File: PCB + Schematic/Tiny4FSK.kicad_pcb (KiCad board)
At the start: 4 copper layers, 30.9 x 65.8 mm, 81 parts, among them IC1 SI4063, J1 SWD, J2 GPIO, J3 USBC, J4 OPTIONAL, J5 I2C, J6 Power, J7 SPI, SW1 RST, SW2 BATT PWR, U1 BME280, U2 MAX-M10S, U3 Linear Step-Down, U4 ATSAMD21G18A-A, U5 TCXO MCU, U6 TPS61200DRC

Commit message: Rebase Rev. 4 PCB files
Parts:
- removed the C11 at (151.0, 99.8)
- removed the C15 at (148.2, 112.0)
- removed the C26 at (144.1, 123.0)
- removed the C4 at (151.1, 88.4)
- removed the C5 at (151.1, 90.5)
- removed the C6 at (148.2, 93.2)
- removed the G*** at (151.2, 102.8)
- removed the G*** at (151.1, 90.5)
- removed the G*** at (142.5, 127.5)
- removed the G*** at (153.0, 127.5)
- removed the J1 at (140.0, 73.5)
- removed JP2: Source, Jumper:SolderJumper-3_P1.3mm_Open_Pad1.0x1.5mm_NumberLabels
- removed the R3 at (151.1, 92.6)
- removed the R7 at (147.7, 100.7)
- removed the U3 at (143.9, 88.1)
- added C13: 100nF, Capacitor_SMD:C_0402_1005Metric_Pad0.74x0.62mm_HandSolder, F.Cu at (158.0, 58.6)
- added C17: 100 nF, Capacitor_SMD:C_0402_1005Metric_Pad0.74x0.62mm_HandSolder, F.Cu at (127.9, 92.7)
- added C18: 1uF, Capacitor_SMD:C_0402_1005Metric_Pad0.74x0.62mm_HandSolder, F.Cu at (129.9, 92.7)
- added C19: 4.7 nF, Capacitor_SMD:C_0402_1005Metric_Pad0.74x0.62mm_HandSolder, F.Cu at (135.9, 98.0)
- added C22: 1uF, Capacitor_SMD:C_0402_1005Metric_Pad0.74x0.62mm_HandSolder, F.Cu at (132.4, 95.1)
- added C25: 100 nF, Capacitor_SMD:C_0402_1005Metric_Pad0.74x0.62mm_HandSolder, F.Cu at (130.5, 98.2)
- added C28: 1.5pF, Capacitor_SMD:C_0402_1005Metric_Pad0.74x0.62mm_HandSolder, F.Cu at (151.7, 42.9)
- added C29: 100nF, Capacitor_SMD:C_0402_1005Metric_Pad0.74x0.62mm_HandSolder, F.Cu at (150.7, 73.3)
- added C30: 100 nF, Capacitor_SMD:C_0402_1005Metric_Pad0.74x0.62mm_HandSolder, F.Cu at (143.9, 78.2)
- added G***: LOGO, LOGO, B.Cu at (144.4, 41.0)
- added G***: LOGO, LOGO, B.Cu at (149.1, 80.1)
- added G***: LOGO, LOGO, B.Cu at (159.3, 41.5)
- added G***: LOGO, LOGO, B.Cu at (149.1, 67.5)
- added G***: LOGO, LOGO, B.Cu at (144.7, 43.1)
- added G***: LOGO, LOGO, B.Cu at (144.7, 45.4)
- added J6: SPI, Connector_PinHeader_2.54mm:PinHeader_1x05_P2.54mm_Vertical, F.Cu at (160.4, 94.1)
- added J8: SWD, Connector_PinHeader_1.27mm:PinHeader_2x05_P1.27mm_Vertical_SMD, B.Cu at (144.8, 103.8)
- added L8: 3.9 nH, Inductor_SMD:L_0402_1005Metric_Pad0.77x0.64mm_HandSolder, F.Cu at (153.2, 43.7)
- added R10: 5k1, Resistor_SMD:R_0402_1005Metric_Pad0.72x0.64mm_HandSolder, F.Cu at (134.0, 98.0)
- added R11: 1M, Resistor_SMD:R_0402_1005Metric_Pad0.72x0.64mm_HandSolder, F.Cu at (136.9, 98.0)
- added R12: 5k1, Resistor_SMD:R_0402_1005Metric_Pad0.72x0.64mm_HandSolder, F.Cu at (132.9, 98.1)
- added R6: 1M, Resistor_SMD:R_0402_1005Metric_Pad0.72x0.64mm_HandSolder, F.Cu at (145.7, 75.7)
- added U7: Linear Step-Down, LDO:MCP1700, F.Cu at (133.5, 92.1)
- AE1: value GPS ANT -> 1575AT43A0040
- AE2: value ANT -> TX Antenna
- BT1: value AAA -> BK-53; footprint BatteryExtended:BAT_BK-82 -> BatteryExtended:BAT_53
- C1: value 1uF -> 10uF; footprint Capacitor_SMD:C_0805_2012Metric_Pad1.18x1.45mm_HandSolder -> Capacitor_SMD:C_0402_1005Metric_Pad0.74x0.62mm_HandSolder
- C10: renamed from C9; value 100nF -> 100 nF; footprint Capacitor_SMD:C_0805_2012Metric_Pad1.18x1.45mm_HandSolder -> Capacitor_SMD:C_0402_1005Metric_Pad0.74x0.62mm_HandSolder
- C11: renamed from C10; footprint Capacitor_SMD:C_0805_2012Metric_Pad1.18x1.45mm_HandSolder -> Capacitor_SMD:C_0402_1005Metric_Pad0.74x0.62mm_HandSolder
- C12: renamed from C7; value 100nF -> 10 uF; footprint Capacitor_SMD:C_0805_2012Metric_Pad1.18x1.45mm_HandSolder -> Capacitor_SMD:C_0402_1005Metric_Pad0.74x0.62mm_HandSolder
- C14, C2, C3: footprint Capacitor_SMD:C_0805_2012Metric_Pad1.18x1.45mm_HandSolder -> Capacitor_SMD:C_0402_1005Metric_Pad0.74x0.62mm_HandSolder
- C16: renamed from C20; footprint Capacitor_SMD:C_0603_1608Metric_Pad1.08x0.95mm_HandSolder -> Capacitor_SMD:C_0402_1005Metric_Pad0.74x0.62mm_HandSolder
- C20: renamed from C22; value 15 pF -> 8 pF; footprint Capacitor_SMD:C_0201_0603Metric_Pad0.64x0.40mm_HandSolder -> Capacitor_SMD:C_0402_1005Metric_Pad0.74x0.62mm_HandSolder
- C21: renamed from C23; footprint Capacitor_SMD:C_0805_2012Metric_Pad1.18x1.45mm_HandSolder -> Capacitor_SMD:C_0402_1005Metric_Pad0.74x0.62mm_HandSolder
- C23: renamed from C18; footprint Capacitor_SMD:C_0805_2012Metric_Pad1.18x1.45mm_HandSolder -> Capacitor_SMD:C_0402_1005Metric_Pad0.74x0.62mm_HandSolder
- C24: renamed from C25; value 12 pF -> 6 pF
- C26: renamed from C24; value 10 nF -> 100 nF; footprint Capacitor_SMD:C_0805_2012Metric_Pad1.18x1.45mm_HandSolder -> Capacitor_SMD:C_0402_1005Metric_Pad0.74x0.62mm_HandSolder
- C27: value 10 pF -> 5 pF; footprint Capacitor_SMD:C_0201_0603Metric_Pad0.64x0.40mm_HandSolder -> Capacitor_SMD:C_0402_1005Metric_Pad0.74x0.62mm_HandSolder
- C4: renamed from C17; footprint Capacitor_SMD:C_0805_2012Metric_Pad1.18x1.45mm_HandSolder -> Capacitor_SMD:C_0603_1608Metric_Pad1.08x0.95mm_HandSolder
- C5: renamed from C21; footprint Capacitor_SMD:C_0805_2012Metric_Pad1.18x1.45mm_HandSolder -> Capacitor_SMD:C_0402_1005Metric_Pad0.74x0.62mm_HandSolder
- C6: renamed from C12; value 10uF -> 100 nF; footprint Capacitor_SMD:C_0805_2012Metric_Pad1.18x1.45mm_HandSolder -> Capacitor_SMD:C_0402_1005Metric_Pad0.74x0.62mm_HandSolder
- C7: renamed from C13; value 100nF -> 10 uF; footprint Capacitor_SMD:C_0805_2012Metric_Pad1.18x1.45mm_HandSolder -> Capacitor_SMD:C_0603_1608Metric_Pad1.08x0.95mm_HandSolder
- C8: renamed from C16; footprint Capacitor_SMD:C_0805_2012Metric_Pad1.18x1.45mm_HandSolder -> Capacitor_SMD:C_0402_1005Metric_Pad0.74x0.62mm_HandSolder
- C9: renamed from C8; footprint Capacitor_SMD:C_0805_2012Metric_Pad1.18x1.45mm_HandSolder -> Capacitor_SMD:C_0402_1005Metric_Pad0.74x0.62mm_HandSolder
- J1: renamed from J6; value Power -> Power Ext
- J3: value USBC -> I2C; footprint Connector_USB:USB_C_Receptacle_GCT_USB4105-xx-A_16P_TopMnt_Horizontal -> Connector_PinHeader_2.54mm:PinHeader_1x04_P2.54mm_Vertical
- J4: value OPTIONAL -> USB; footprint Jumper:SolderJumper-2_P1.3mm_Open_Pad1.0x1.5mm -> Connector_PinHeader_2.54mm:PinHeader_1x04_P2.54mm_Vertical
- J5: value I2C -> USB Breakout
- J7: value SPI -> USBC; footprint Connector_PinHeader_2.54mm:PinHeader_1x05_P2.54mm_Vertical -> Connector_USB:USB_C_Receptacle_GCT_USB4105-xx-A_16P_TopMnt_Horizontal
- JP1: value SWITCH_EN -> Switch EN
- L1: value 33 nH -> 3.9 nH
- L3: footprint Inductor_SMD:L_0603_1608Metric_Pad1.05x0.95mm_HandSolder -> Inductor_SMD:L_0402_1005Metric_Pad0.77x0.64mm_HandSolder
- L4: value 33 nH -> 14 nH
- L5: value 30 nH -> 14 nH
- L6: value 36 nH -> 14 nH
- L7: value 22 nH -> 14 nH
- R1: renamed from R2; footprint Resistor_SMD:R_0805_2012Metric_Pad1.20x1.40mm_HandSolder -> Resistor_SMD:R_0402_1005Metric_Pad0.72x0.64mm_HandSolder
- R13: renamed from R10; value 100 -> 330; footprint Resistor_SMD:R_0805_2012Metric_Pad1.20x1.40mm_HandSolder -> Resistor_SMD:R_0402_1005Metric_Pad0.72x0.64mm_HandSolder
- R14: renamed from R13; value 1k -> 330; footprint Resistor_SMD:R_0805_2012Metric_Pad1.20x1.40mm_HandSolder -> Resistor_SMD:R_0402_1005Metric_Pad0.72x0.64mm_HandSolder
- R15: renamed from R9; value 100 -> 330; footprint Resistor_SMD:R_0805_2012Metric_Pad1.20x1.40mm_HandSolder -> Resistor_SMD:R_0402_1005Metric_Pad0.72x0.64mm_HandSolder
- R2: renamed from R1; footprint Resistor_SMD:R_0805_2012Metric_Pad1.20x1.40mm_HandSolder -> Resistor_SMD:R_0402_1005Metric_Pad0.72x0.64mm_HandSolder
- R3: renamed from R12; value 5M -> 1M; footprint Resistor_SMD:R_0805_2012Metric_Pad1.20x1.40mm_HandSolder -> Resistor_SMD:R_0402_1005Metric_Pad0.72x0.64mm_HandSolder
- R4: renamed from R11; value 900k -> 180k; footprint Resistor_SMD:R_0805_2012Metric_Pad1.20x1.40mm_HandSolder -> Resistor_SMD:R_0402_1005Metric_Pad0.72x0.64mm_HandSolder
- R5: value 5k1 -> 1M; footprint Resistor_SMD:R_0805_2012Metric_Pad1.20x1.40mm_HandSolder -> Resistor_SMD:R_0402_1005Metric_Pad0.72x0.64mm_HandSolder
- R7: renamed from R4; footprint Resistor_SMD:R_0805_2012Metric_Pad1.20x1.40mm_HandSolder -> Resistor_SMD:R_0402_1005Metric_Pad0.72x0.64mm_HandSolder
- R8: renamed from R6; footprint Resistor_SMD:R_0805_2012Metric_Pad1.20x1.40mm_HandSolder -> Resistor_SMD:R_0402_1005Metric_Pad0.72x0.64mm_HandSolder
- R9: renamed from R8; footprint Resistor_SMD:R_0805_2012Metric_Pad1.20x1.40mm_HandSolder -> Resistor_SMD:R_0402_1005Metric_Pad0.72x0.64mm_HandSolder
- SW1: renamed from SW2; value BATT PWR -> Power Switch; footprint SlideSwitch:WS-SLSU_6p7x2p7_WRE -> Button_Switch_SMD:SW_SPDT_PCM12
- U2: value MAX-M10S -> ATGM336H; footprint RF_GPS:ublox_MAX -> RF_GPS_Extended:ATGM336H
- U4: renamed from U5; value TCXO MCU -> ECS-327TXO-2012; footprint Oscillator_TCXO:ATXK-H11-E-32.768KHZ-E50-T3 -> Oscillator_TCXO:ECS-327TXO-2012
- U8: renamed from XTAL1; footprint OSC:OSC_ECS-TXO-32CSMV-260-AN-TR -> Oscillator_TCXO:ECS-TXO-20CSMV4
- moved H3 62.8 mm to (115.0, 64.7)
- moved JP1 60.3 mm to (145.4, 63.6), turned to 90 degrees
- moved SW1 60.3 mm to (142.5, 69.8), turned to -90 degrees
- moved C5 51.9 mm to (155.9, 66.5), turned to 0 degrees
- moved C4 51.0 mm to (155.4, 65.3), turned to 0 degrees
- moved H2 48.2 mm to (159.1, 45.9)
- moved R4 47.9 mm to (155.2, 72.4), turned to 0 degrees
- moved J1 47.9 mm to (142.3, 63.5), turned to 180 degrees
- moved R3 47.4 mm to (153.0, 72.4), turned to 0 degrees
- moved C8 45.5 mm to (156.4, 69.8), turned to -90 degrees
- moved BT1 44.3 mm to (150.2, 74.9), turned to -90 degrees
- moved L2 42.3 mm to (150.8, 65.0), turned to 180 degrees
- moved U3 41.5 mm to (153.6, 69.8), turned to -90 degrees
- moved L1 38.8 mm to (151.0, 41.2), turned to -135 degrees
- moved C7 37.2 mm to (149.1, 69.8), turned to -90 degrees
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- renumbered C19 to C15, SW1 to SW2, U6 to U3, U4 to U5, IC1 to U6
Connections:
- net EXTINT renamed GPS_EN
- AE1 pad 1: ANT_GPS -> Net-(AE1-A)
- C1 pad 2: LIN -> +3.3V
- C3 pad 1: LDO -> +BATT
- C4 pad 1: BOOST -> +3.3V
- C5 pad 1: BOOST -> +3.3V
- D1 pad 1: Earth -> Net-(D1-K)
- D1 pad 2: Net-(D1-A) -> SUCCESS
- D2 pad 1: Earth -> Net-(D2-K)
- D2 pad 2: Net-(D2-A) -> ERROR
- D3 pad 1: Earth -> Net-(D3-K)
- D3 pad 2: Net-(D3-A) -> +3.3V
- J1 pad 1: BATT_SENSE -> +BATT
- J4 pad 1: TCXO -> D+
- J4 pad 2: OPT XOUT -> D-
- J5 pad 1: +3.3V -> D+
- J5 pad 2: SDA -> D-
- J5 pad 3: SCL -> +3.3V
- JP1 pad 2: BATT_SENSE -> +BATT
- L1 pad 2: ANT_GPS -> Net-(AE1-A)
- R13 pad 1: ERROR -> Net-(D2-K)
- R13 pad 2: Net-(D2-A) -> Earth
- R14 pad 1: +3.3V -> Net-(D3-K)
- R14 pad 2: Net-(D3-A) -> Earth
- R15 pad 1: Net-(D1-A) -> Net-(D1-K)
- R15 pad 2: SUCCESS -> Earth
- R3 pad 1: BOOST -> +3.3V
- R5 pad 1: Earth -> +BATT
- R5 pad 2: Net-(J3-CC1) -> BATT_SENSE
- R8 pad 1: SCL -> +3.3V
- R8 pad 2: +3.3V -> SCL
- SW1 pad 1: BATT_SENSE -> +BATT
- U2 pad 16: SDA -> unconnected-(U2-SDA-Pad16)
- U2 pad 17: SCL -> unconnected-(U2-SCL-Pad17)
- U2 pad 2: unconnected-(U2-TXD-Pad2) -> RXD
- U2 pad 3: unconnected-(U2-RXD-Pad3) -> TXD
- U2 pad 6: unconnected-(U2-V_BCKP-Pad6) -> +3.3V
- U2 pad 7: +3.3V -> unconnected-(U2-NC-Pad7)
- U3 pad 2: BOOST -> +3.3V
- U4 pad 3: Net-(U5-OUTPUT) -> TCXO
- U5 pad 15: unconnected-(U4-PA10-Pad15) -> TXD
- U5 pad 16: unconnected-(U4-PA11-Pad16) -> RXD
- U5 pad 2: OPT XOUT -> unconnected-(U5-PA01-Pad2)
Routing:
- net Earth: track 106.9 -> 36.0 mm, vias 95 -> 150
- net BATT_SENSE: track 70.9 -> 8.07 mm, vias 5 -> 0
- net RXD: track 0.00 -> 48.7 mm, vias 0 -> 2
- net LDO: track 47.4 -> 0.00 mm, vias 2 -> 0
- net TXD: track 0.00 -> 46.7 mm, vias 0 -> 2
- net BST_IN: track 45.1 -> 14.8 mm
- net +BATT: track 0.00 -> 30.2 mm, vias 0 -> 5
- net Net-(J3-SHIELD): track 28.6 -> 0.00 mm, vias 1 -> 0
- net ERROR: track 2.14 -> 28.3 mm, vias 0 -> 4
- net BOOST: track 22.1 -> 0.00 mm
- net SUCCESS: track 1.96 -> 23.4 mm, vias 0 -> 2
- net Net-(J7-SHIELD): track 0.00 -> 19.9 mm
- net GPS_EN: track 28.8 -> 48.2 mm
- net SWDIO: track 45.2 -> 26.4 mm
- net SWCLK: track 45.9 -> 28.7 mm
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- added copper zone on F.Cu, net BST_IN
- added copper zone on B.Cu, net Earth
- removed copper zone on F.Cu, net BOOST
- removed copper zone on F.Cu, net Net-(U3-L)
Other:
- board size 30.9 x 65.8 mm -> 35.1 x 73.6 mm
- board text added: "Licensed under CERN-OHL-W-2.0"
- board text added: "Made by Max Kendall, W0MXX"
- board text added: "Max W0MXX"
- board text added: "November 2024"
- board text added: "Rev. 4.0"
- board text added: "Sponsored by:"
- board text added: "USB Breakout"
- board text added: "WayWayWay"
- board text removed: "+"
- board text removed: "-"
- board text removed: "BST"
- board text removed: "Developed by Max W0MXX"
- board text removed: "JP1 - Cut to enable SW2 for PWR JP2 - Control PWR source (USB and CTR for USB, CTR and BATT) SW1 - RST SW2 - BATT PWR AE2 - 70cm ANT"
- board text removed: "RST"
- board text removed: "Rev. 3 - 4/19/24"
- board text removed: "SW CTRL"
- board text removed: "SWCLK"
- board text removed: "SWDIO"
- board text removed: "USB BATT"

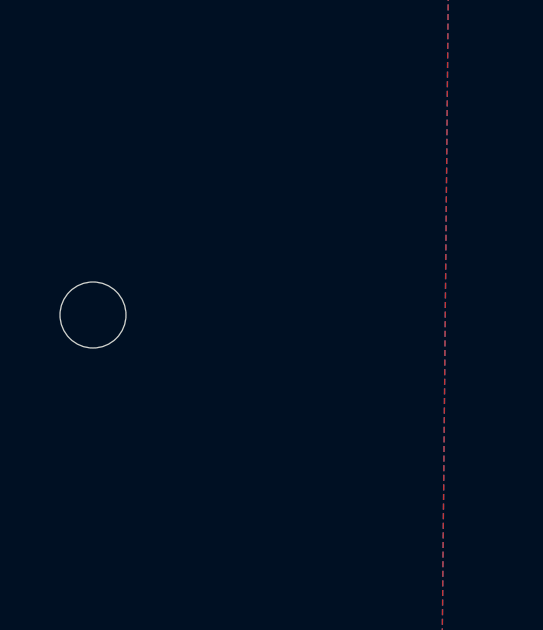
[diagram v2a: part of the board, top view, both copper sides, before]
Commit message: revert kicad version to 8
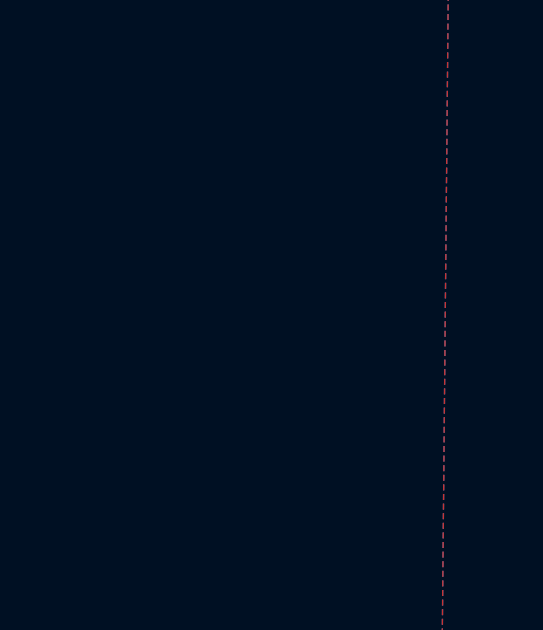
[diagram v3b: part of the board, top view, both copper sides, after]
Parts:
- removed H3: MountingHole, MountingHole:MountingHole_2.2mm_M2
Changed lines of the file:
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@@
 			(thermal_bridge_angle 45)
 		)
-		(model "${KIPRJMOD}/3D/CM7V-T1A-32.768K-12.5PF-20PPM-TA-QA.step"
-			(offset
-				(xyz 0 0 0)
-			)
-			(scale
-				(xyz 1 1 1)
-			)
-			(rotate
-				(xyz -90 0 0)
-			)
-		)
 	)
 	(footprint "Connector_USB:USB_C_Receptacle_GCT_USB4105-xx-A_16P_TopMnt_Horizontal"
@@
 			(pintype "no_connect")
 		)
-		(model "${KIPRJMOD}/3D/User Library-MAX-M8 u-blox M8 Concurrent GNSS Module.step"
+		(model "C:/Users/maxsr/Downloads/User Library-MAX-M8 u-blox M8 Concurrent GNSS Module.step"
 			(offset
 				(xyz 0 0 0)
@@
 		)
 	)
-	(footprint "MountingHole:MountingHole_2.2mm_M2"
-		(layer "F.Cu")
-		(at 114.975 64.675)
-		(descr "Mounting Hole 2.2mm, no annular, M2")
-		(tags "mounting hole 2.2mm no annular m2")
-		(property "Reference" "H3"
-			(at 0 -3.2 0)
-			(layer "F.SilkS")
-			(hide yes)
-			(effects
-				(font
-					(size 1 1)
-					(thickness 0.15)
-				)
-			)
-		)
-		(property "Value" "MountingHole"
-			(at 0 3.2 0)
-			(layer "F.Fab")
-			(effects
-				(font
-					(size 1 1)
-					(thickness 0.15)
-				)
-			)
-		)
-		(property "Footprint" "MountingHole:MountingHole_2.2mm_M2"
-			(at 0 0 0)
-			(unlocked yes)
-			(layer "F.Fab")
-			(hide yes)
-			(effects
-				(font
-					(size 1.27 1.27)
-					(thickness 0.15)
-				)
-			)
-		)
-		(property "Datasheet" ""
-			(at 0 0 0)
-			(unlocked yes)
-			(layer "F.Fab")
-			(hide yes)
-			(effects
-				(font
-					(size 1.27 1.27)
-					(thickness 0.15)
-				)
-			)
-		)
-		(property "Description" "Mounting Hole without connection"
-			(at 0 0 0)
-			(unlocked yes)
-			(layer "F.Fab")
-			(hide yes)
-			(effects
-				(font
-					(size 1.27 1.27)
-					(thickness 0.15)
-				)
-			)
-		)
-		(property ki_fp_filters "MountingHole*")
-		(sheetname "Root")
-		(sheetfile "Tiny4FSK.kicad_sch")
-		(attr exclude_from_pos_files exclude_from_bom)
-		(fp_circle
-			(center 0 0)
-			(end 2.2 0)
-			(stroke
-				(width 0.15)
-				(type solid)
-			)
-			(fill none)
-			(layer "Cmts.User")
-		)
-		(fp_circle
-			(center 0 0)
-			(end 2.45 0)
-			(stroke
-				(width 0.05)
-				(type solid)
-			)
-			(fill none)
-			(layer "F.CrtYd")
-		)
-		(fp_text user "${REFERENCE}"
-			(at 0 0 0)
-			(layer "F.Fab")
-			(effects
-				(font
-					(size 1 1)
-					(thickness 0.15)
-				)
-			)
-		)
-		(pad "" np_thru_hole circle
-			(at 0 0)
-			(size 2.2 2.2)
-			(drill 2.2)
-			(layers "*.Cu" "*.Mask")
-		)
-	)
 	(footprint "Package_LGA:Bosch_LGA-8_2.5x2.5mm_P0.65mm_ClockwisePinNumbering"
 		(layer "F.Cu")
@@
 			)
 		)
-		(model "${KIPRJMOD}/3D/shapes3D/shapes3D/User Library-Bosch_BME280.wrl"
+		(model "C:/Users/maxsr/Downloads/User Library-Bosch_BME280.step"
 			(offset
 				(xyz 0 0 0)
@@
 			)
 			(rotate
-				(xyz -90 0 180)
+				(xyz -90 0 0)
 			)
 		)
@@
 			(pintype "passive")
 		)
-		(model "${KIPRJMOD}/3D/Coilcraft-LPS3015.step"
+		(model "C:/Users/maxsr/Downloads/Coilcraft-LPS3015.step"
 			(offset
 				(xyz 0 0 0)
@@
 			(thermal_bridge_angle 45)
 		)
-		(model "${KIPRJMOD}/3D/CM7V-T1A-32.768K-12.5PF-20PPM-TA-QA.step"
-			(offset
-				(xyz 0 0 0)
-			)
-			(scale
-				(xyz 1 1 1)
-			)
-			(rotate
-				(xyz -90 0 0)
-			)
-		)
 	)
 	(footprint "Resistor_SMD:R_0402_1005Metric_Pad0.72x0.64mm_HandSolder"
@@
 			)
 		)
-		(model "${KIPRJMOD}/3D/ANT_1575AT_JOT.step"
+		(model "C:/Users/maxsr/Downloads/1575AT43A0040E/ANT_1575AT_JOT.step"
 			(offset
 				(xyz 0 0 0)

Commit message: update 3d model paths
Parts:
- added H3: MountingHole, MountingHole:MountingHole_2.2mm_M2, F.Cu at (115.0, 64.7)
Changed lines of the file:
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@@
 			(thermal_bridge_angle 45)
 		)
+		(model "${KIPRJMOD}/3D/CM7V-T1A-32.768K-12.5PF-20PPM-TA-QA.step"
+			(offset
+				(xyz 0 0 0)
+			)
+			(scale
+				(xyz 1 1 1)
+			)
+			(rotate
+				(xyz -90 0 0)
+			)
+		)
 	)
 	(footprint "Connector_USB:USB_C_Receptacle_GCT_USB4105-xx-A_16P_TopMnt_Horizontal"
@@
 			(pintype "no_connect")
 		)
-		(model "C:/Users/maxsr/Downloads/User Library-MAX-M8 u-blox M8 Concurrent GNSS Module.step"
+		(model "${KIPRJMOD}/3D/User Library-MAX-M8 u-blox M8 Concurrent GNSS Module.step"
 			(offset
 				(xyz 0 0 0)
@@
 		)
 	)
+	(footprint "MountingHole:MountingHole_2.2mm_M2"
+		(layer "F.Cu")
+		(at 114.975 64.675)
+		(descr "Mounting Hole 2.2mm, no annular, M2")
+		(tags "mounting hole 2.2mm no annular m2")
+		(property "Reference" "H3"
+			(at 0 -3.2 0)
+			(layer "F.SilkS")
+			(hide yes)
+			(effects
+				(font
+					(size 1 1)
+					(thickness 0.15)
+				)
+			)
+		)
+		(property "Value" "MountingHole"
+			(at 0 3.2 0)
+			(layer "F.Fab")
+			(effects
+				(font
+					(size 1 1)
+					(thickness 0.15)
+				)
+			)
+		)
+		(property "Footprint" "MountingHole:MountingHole_2.2mm_M2"
+			(at 0 0 0)
+			(unlocked yes)
+			(layer "F.Fab")
+			(hide yes)
+			(effects
+				(font
+					(size 1.27 1.27)
+					(thickness 0.15)
+				)
+			)
+		)
+		(property "Datasheet" ""
+			(at 0 0 0)
+			(unlocked yes)
+			(layer "F.Fab")
+			(hide yes)
+			(effects
+				(font
+					(size 1.27 1.27)
+					(thickness 0.15)
+				)
+			)
+		)
+		(property "Description" "Mounting Hole without connection"
+			(at 0 0 0)
+			(unlocked yes)
+			(layer "F.Fab")
+			(hide yes)
+			(effects
+				(font
+					(size 1.27 1.27)
+					(thickness 0.15)
+				)
+			)
+		)
+		(property ki_fp_filters "MountingHole*")
+		(sheetname "Root")
+		(sheetfile "Tiny4FSK.kicad_sch")
+		(attr exclude_from_pos_files exclude_from_bom)
+		(fp_circle
+			(center 0 0)
+			(end 2.2 0)
+			(stroke
+				(width 0.15)
+				(type solid)
+			)
+			(fill none)
+			(layer "Cmts.User")
+		)
+		(fp_circle
+			(center 0 0)
+			(end 2.45 0)
+			(stroke
+				(width 0.05)
+				(type solid)
+			)
+			(fill none)
+			(layer "F.CrtYd")
+		)
+		(fp_text user "${REFERENCE}"
+			(at 0 0 0)
+			(layer "F.Fab")
+			(effects
+				(font
+					(size 1 1)
+					(thickness 0.15)
+				)
+			)
+		)
+		(pad "" np_thru_hole circle
+			(at 0 0)
+			(size 2.2 2.2)
+			(drill 2.2)
+			(layers "*.Cu" "*.Mask")
+		)
+	)
 	(footprint "Package_LGA:Bosch_LGA-8_2.5x2.5mm_P0.65mm_ClockwisePinNumbering"
 		(layer "F.Cu")
@@
 			)
 		)
-		(model "C:/Users/maxsr/Downloads/User Library-Bosch_BME280.step"
+		(model "${KIPRJMOD}/3D/shapes3D/shapes3D/User Library-Bosch_BME280.wrl"
 			(offset
 				(xyz 0 0 0)
@@
 			)
 			(rotate
-				(xyz -90 0 0)
+				(xyz -90 0 180)
 			)
 		)
@@
 			(pintype "passive")
 		)
-		(model "C:/Users/maxsr/Downloads/Coilcraft-LPS3015.step"
+		(model "${KIPRJMOD}/3D/Coilcraft-LPS3015.step"
 			(offset
 				(xyz 0 0 0)
@@
 			(thermal_bridge_angle 45)
 		)
+		(model "${KIPRJMOD}/3D/CM7V-T1A-32.768K-12.5PF-20PPM-TA-QA.step"
+			(offset
+				(xyz 0 0 0)
+			)
+			(scale
+				(xyz 1 1 1)
+			)
+			(rotate
+				(xyz -90 0 0)
+			)
+		)
 	)
 	(footprint "Resistor_SMD:R_0402_1005Metric_Pad0.72x0.64mm_HandSolder"
@@
 			)
 		)
-		(model "C:/Users/maxsr/Downloads/1575AT43A0040E/ANT_1575AT_JOT.step"
+		(model "${KIPRJMOD}/3D/ANT_1575AT_JOT.step"
 			(offset
 				(xyz 0 0 0)

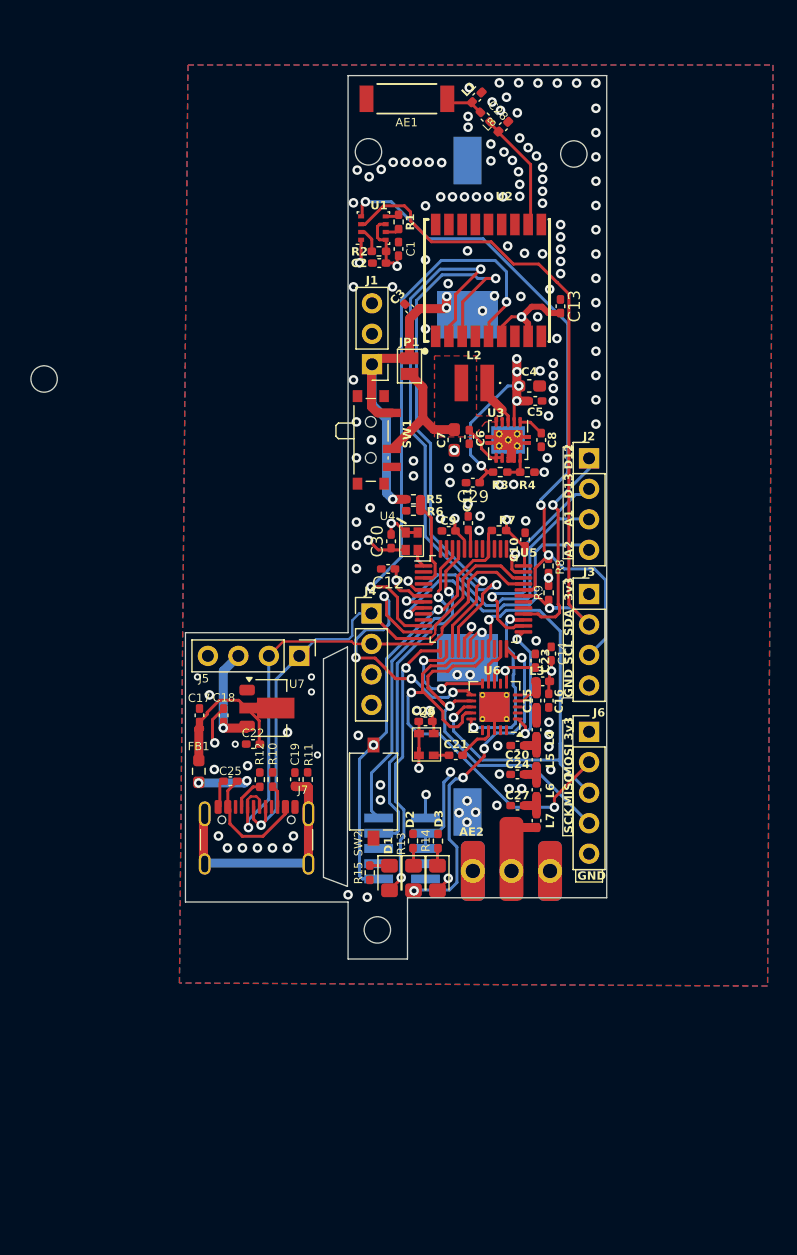
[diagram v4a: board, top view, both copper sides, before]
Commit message: increase battery spacing, revamp silkscreen
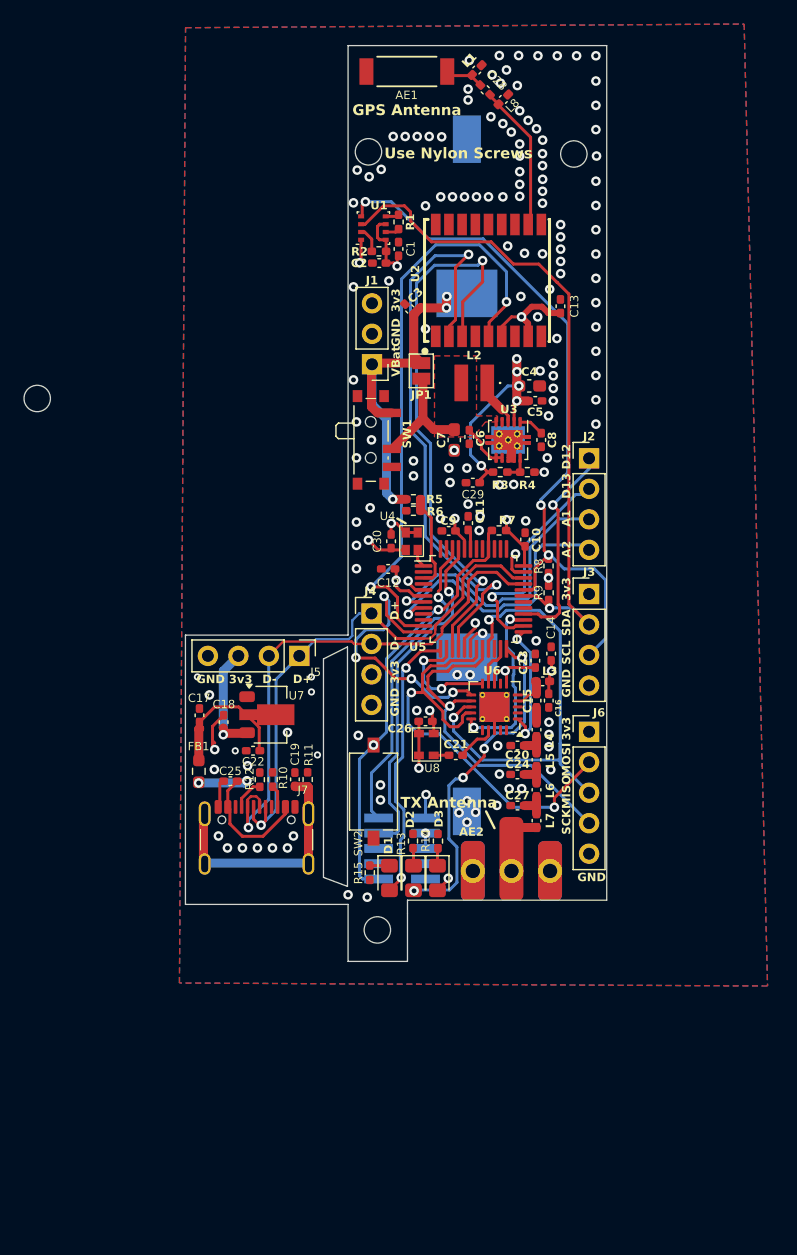
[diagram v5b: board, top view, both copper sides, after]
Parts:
- removed the G*** at (149.1, 67.5)
- added G***: LOGO, LOGO, B.Cu at (150.7, 66.2)
- added G***: LOGO, LOGO, B.Cu at (150.5, 81.1)
- moved G*** 3.12 mm to (150.7, 77.4)
- moved G*** 2.27 mm to (159.3, 39.2)
- moved AE1 2.27 mm to (145.2, 39.1)
- moved C28 2.27 mm to (151.7, 40.6)
- moved G*** 2.27 mm to (144.4, 38.8)
- moved G*** 2.27 mm to (144.7, 40.9)
- moved G*** 2.27 mm to (144.7, 43.1)
- moved L1 2.27 mm to (151.0, 38.9)
- moved L8 2.27 mm to (153.2, 41.4)
- moved BT1 1.78 mm to (150.2, 73.1)
- moved H3 1.72 mm to (114.4, 66.3)
- moved JP1 1.06 mm to (146.4, 64.0)
- moved C18 0.56 mm to (129.9, 93.3)
- moved C22 0.56 mm to (132.4, 95.6)
- moved U7 0.56 mm to (133.5, 92.6)
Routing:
- net Earth: track 36.0 -> 28.9 mm, vias 150 -> 151
- net ANT_GPS: track 10.2 -> 12.5 mm
- net GPS_EN: track 48.2 -> 50.3 mm
- net +BATT: track 30.2 -> 31.5 mm, vias 5 -> 3
- net RXD: track 48.7 -> 49.9 mm
- net BST_IN: track 14.8 -> 13.9 mm
- net TXD: track 46.7 -> 47.4 mm
- net SDA: track 56.8 -> 56.2 mm
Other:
- board size 35.1 x 73.6 mm -> 35.1 x 76.3 mm
- board text added: "D+"
- board text added: "D-"
- board text added: "GPS Antenna"
- board text added: "January 2025"
- board text added: "Rev. 4.1"
- board text added: "TX Antenna"
- board text added: "Use Nylon Screws"
- board text added: "VBat"
- board text removed: "November 2024"
- board text removed: "Rev. 4.0"
